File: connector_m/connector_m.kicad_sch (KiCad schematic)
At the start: 33 parts, among them J1 PowerOut, J2 PowerIn, J3 CANFD_In, U1 SKA2P1_TX, U2 TJA1042T, U3 SKA2P1_RX, U5 XC6206P182MR, U6 LSF0102DCUR

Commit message: [New] Add connector m
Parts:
- J1: footprint Rolling_Custom:POGOPIN-2PAD -> Rolling_Custom:POGOPIN-E21160-ASB-2PIN
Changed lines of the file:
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@@
       (effects (font (size 1.27 1.27)) (justify left))
     )
-    (property "Footprint" "Rolling_Custom:POGOPIN-2PAD" (id 2) (at 31.75 118.11 0)
+    (property "Footprint" "Rolling_Custom:POGOPIN-E21160-ASB-2PIN" (id 2) (at 31.75 118.11 0)
       (effects (font (size 1.27 1.27)) hide)
     )
@@
     )
     (path "/4eb1718d-60e2-494b-95fa-12d2aa3e9de5"
-      (reference "J1") (unit 1) (value "PowerOut") (footprint "Rolling_Custom:POGOPIN-2PAD")
+      (reference "J1") (unit 1) (value "PowerOut") (footprint "Rolling_Custom:POGOPIN-E21160-ASB-2PIN")
     )
     (path "/c77e216b-0ed3-4756-9a22-7960f03f738d"

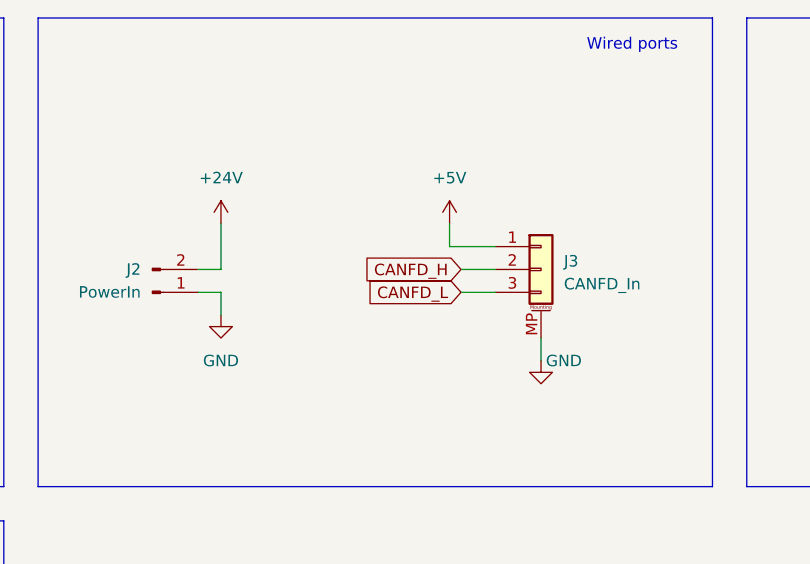
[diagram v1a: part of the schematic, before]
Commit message: [Modify] Change CAN ports sequence
2pin: 1-CAN_L, 2-CAN_H
3pin: 1-5V, 2-CAN_L, 3-CAN_H
4pin: 1,2-CAN_L, 3,4-CAN_H

Signed-off-by: Homalozoa <nx.tardis@gmail.com>
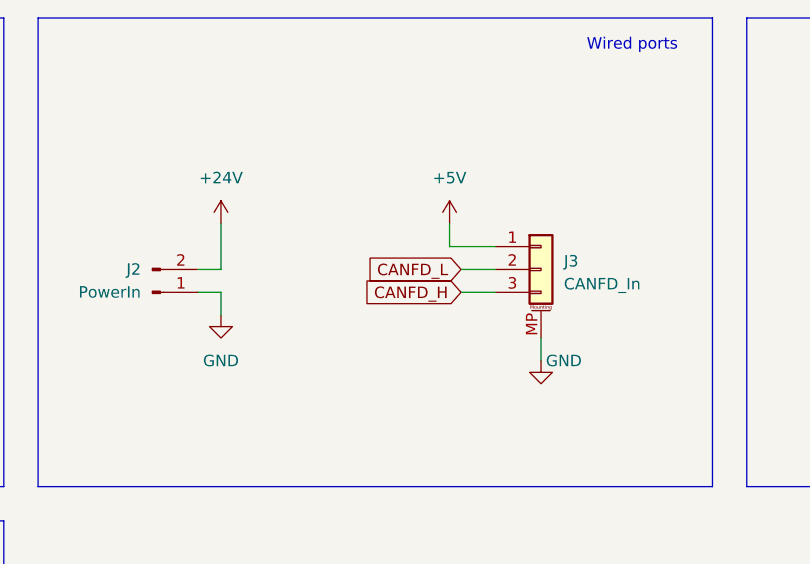
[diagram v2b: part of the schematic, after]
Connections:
- net CANFD_H: now also J3.3 (Pin_3); no longer J3.2 (Pin_2)
- net CANFD_L: now also J3.2 (Pin_2); no longer J3.3 (Pin_3)

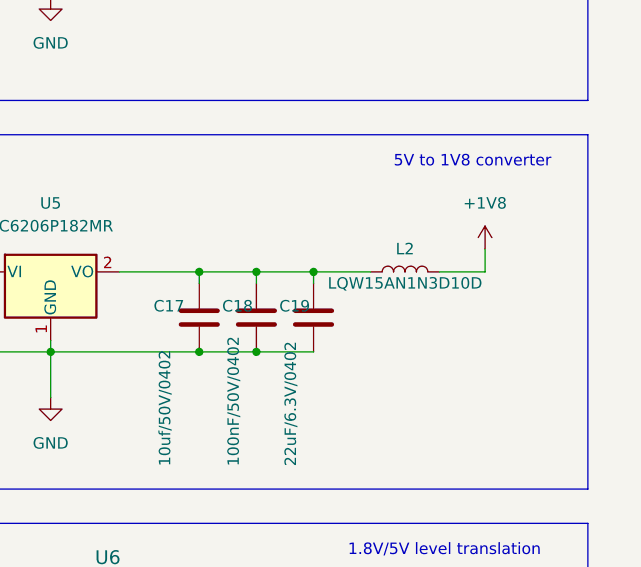
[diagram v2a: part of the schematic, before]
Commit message: [Fix] Manufacture modification
Signed-off-by: Homalozoa <nx.tardis@gmail.com>
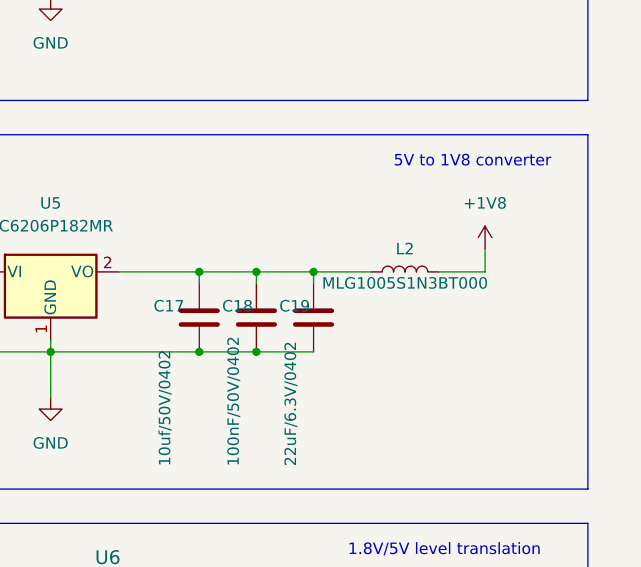
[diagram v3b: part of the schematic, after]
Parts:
- L2: value LQW15AN1N3D10D -> MLG1005S1N3BT000
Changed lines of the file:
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@@
     (in_bom yes) (on_board yes)
     (property "Reference" "L2" (id 0) (at 259.08 86.36 90))
-    (property "Value" "LQW15AN1N3D10D" (id 1) (at 259.08 90.17 90))
+    (property "Value" "MLG1005S1N3BT000" (id 1) (at 259.08 90.17 90))
     (property "Footprint" "Inductor_SMD:L_0402_1005Metric" (id 2) (at 259.08 88.9 0)
       (effects (font (size 1.27 1.27)) hide)
@@
     )
     (path "/d4458d1c-7910-440e-8dea-d1e03df2f9b3"
-      (reference "L2") (unit 1) (value "LQW15AN1N3D10D") (footprint "Inductor_SMD:L_0402_1005Metric")
+      (reference "L2") (unit 1) (value "MLG1005S1N3BT000") (footprint "Inductor_SMD:L_0402_1005Metric")
     )
     (path "/54e6f392-5199-47aa-b110-24d3a39b268d"
